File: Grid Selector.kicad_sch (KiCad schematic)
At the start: 122 parts, among them SW1 MX_SW_HS, SW10 MX_SW_HS, SW11 MX_SW_HS, SW12 MX_SW_HS, SW13 MX_SW_HS, SW14 MX_SW_HS, SW15 MX_SW_HS, SW16 MX_SW_HS, SW17 MX_SW_HS, SW18 MX_SW_HS, SW19 MX_SW_HS, SW2 MX_SW_HS, SW20 MX_SW_HS, SW21 MX_SW_HS, SW22 MX_SW_HS, SW23 MX_SW_HS, SW24 MX_SW_HS, SW25 MX_SW_HS, SW26 MX_SW_HS, SW27 MX_SW_HS, SW28 MX_SW_HS, SW29 MX_SW_HS, SW3 MX_SW_HS, SW30 MX_SW_HS, SW4 MX_SW_HS, SW5 MX_SW_HS, SW6 MX_SW_HS, SW7 MX_SW_HS, SW8 MX_SW_HS, SW9 MX_SW_HS, U1 Pico

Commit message: cleaned up pcb
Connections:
- net COL0: now also U1.12 (GPIO9); no longer U1.15 (GPIO11)
- net COL1: now also U1.11 (GPIO8); no longer U1.12 (GPIO9)
- net COL2: now also U1.10 (GPIO7); no longer U1.11 (GPIO8)
- net COL3: now also U1.9 (GPIO6); no longer U1.10 (GPIO7)
- net COL4: now also U1.7 (GPIO5); no longer U1.9 (GPIO6)
- net COL5: now also U1.6 (GPIO4); no longer U1.7 (GPIO5)
- net COL6: now also U1.5 (GPIO3); no longer U1.6 (GPIO4)
- net GND: now also U1.18 (GND); no longer U1.8 (GND)
- net ROW0: now also U1.15 (GPIO11); no longer U1.5 (GPIO3)
- net ROW1: now also U1.16 (GPIO12); no longer U1.14 (GPIO10)
- net ROW2: now also U1.17 (GPIO13); no longer U1.20 (GPIO15)
- net LED: now reaches LED1.3 (DIN)
- net LED: now also U1.14 (GPIO10)
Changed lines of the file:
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@@
     (stroke (width 0) (type default) (color 0 0 0 0))
   )
-  (wire (pts (xy 181.61 47.625) (xy 191.135 47.625))
+  (wire (pts (xy 181.61 73.025) (xy 191.135 73.025))
     (stroke (width 0) (type default) (color 0 0 0 0))
   )
@@
     (stroke (width 0) (type default) (color 0 0 0 0))
   )
-  (global_label "COL5" (shape input) (at 191.135 45.085 180) (fields_autoplaced)
-    (effects (font (size 1.27 1.27)) (justify right))
-    (property "Intersheet References" "${INTERSHEET_REFS}" (id 0) (at 183.8838 45.0056 0)
+  (global_label "COL5" (shape input) (at 191.135 42.545 180) (fields_autoplaced)
+    (effects (font (size 1.27 1.27)) (justify right))
+    (property "Intersheet References" "${INTERSHEET_REFS}" (id 0) (at 183.8838 42.4656 0)
       (effects (font (size 1.27 1.27)) (justify right) hide)
     )
@@
     )
   )
-  (global_label "COL1" (shape input) (at 191.135 57.785 180) (fields_autoplaced)
-    (effects (font (size 1.27 1.27)) (justify right))
-    (property "Intersheet References" "${INTERSHEET_REFS}" (id 0) (at 183.8838 57.7056 0)
+  (global_label "COL1" (shape input) (at 191.135 55.245 180) (fields_autoplaced)
+    (effects (font (size 1.27 1.27)) (justify right))
+    (property "Intersheet References" "${INTERSHEET_REFS}" (id 0) (at 183.8838 55.1656 0)
       (effects (font (size 1.27 1.27)) (justify right) hide)
     )
@@
     )
   )
-  (global_label "COL3" (shape input) (at 191.135 52.705 180) (fields_autoplaced)
-    (effects (font (size 1.27 1.27)) (justify right))
-    (property "Intersheet References" "${INTERSHEET_REFS}" (id 0) (at 183.8838 52.6256 0)
+  (global_label "COL3" (shape input) (at 191.135 50.165 180) (fields_autoplaced)
+    (effects (font (size 1.27 1.27)) (justify right))
+    (property "Intersheet References" "${INTERSHEET_REFS}" (id 0) (at 183.8838 50.0856 0)
+      (effects (font (size 1.27 1.27)) (justify right) hide)
+    )
+  )
+  (global_label "LED" (shape input) (at 19.685 102.87 180) (fields_autoplaced)
+    (effects (font (size 1.27 1.27)) (justify right))
+    (property "Intersheet References" "${INTERSHEET_REFS}" (id 0) (at 13.8248 102.7906 0)
       (effects (font (size 1.27 1.27)) (justify right) hide)
     )
@@
     )
   )
-  (global_label "COL2" (shape input) (at 191.135 55.245 180) (fields_autoplaced)
-    (effects (font (size 1.27 1.27)) (justify right))
-    (property "Intersheet References" "${INTERSHEET_REFS}" (id 0) (at 183.8838 55.1656 0)
+  (global_label "COL2" (shape input) (at 191.135 52.705 180) (fields_autoplaced)
+    (effects (font (size 1.27 1.27)) (justify right))
+    (property "Intersheet References" "${INTERSHEET_REFS}" (id 0) (at 183.8838 52.6256 0)
       (effects (font (size 1.27 1.27)) (justify right) hide)
     )
@@
     )
   )
-  (global_label "ROW2" (shape input) (at 191.135 78.105 180) (fields_autoplaced)
-    (effects (font (size 1.27 1.27)) (justify right))
-    (property "Intersheet References" "${INTERSHEET_REFS}" (id 0) (at 183.4605 78.0256 0)
+  (global_label "ROW2" (shape input) (at 191.135 70.485 180) (fields_autoplaced)
+    (effects (font (size 1.27 1.27)) (justify right))
+    (property "Intersheet References" "${INTERSHEET_REFS}" (id 0) (at 183.4605 70.4056 0)
       (effects (font (size 1.27 1.27)) (justify right) hide)
     )
@@
     )
   )
-  (global_label "COL4" (shape input) (at 191.135 50.165 180) (fields_autoplaced)
-    (effects (font (size 1.27 1.27)) (justify right))
-    (property "Intersheet References" "${INTERSHEET_REFS}" (id 0) (at 183.8838 50.0856 0)
-      (effects (font (size 1.27 1.27)) (justify right) hide)
-    )
-  )
-  (global_label "COL6" (shape input) (at 191.135 42.545 180) (fields_autoplaced)
-    (effects (font (size 1.27 1.27)) (justify right))
-    (property "Intersheet References" "${INTERSHEET_REFS}" (id 0) (at 183.8838 42.4656 0)
+  (global_label "LED" (shape input) (at 191.135 62.865 180) (fields_autoplaced)
+    (effects (font (size 1.27 1.27)) (justify right))
+    (property "Intersheet References" "${INTERSHEET_REFS}" (id 0) (at 185.2748 62.7856 0)
+      (effects (font (size 1.27 1.27)) (justify right) hide)
+    )
+  )
+  (global_label "COL4" (shape input) (at 191.135 45.085 180) (fields_autoplaced)
+    (effects (font (size 1.27 1.27)) (justify right))
+    (property "Intersheet References" "${INTERSHEET_REFS}" (id 0) (at 183.8838 45.0056 0)
+      (effects (font (size 1.27 1.27)) (justify right) hide)
+    )
+  )
+  (global_label "COL6" (shape input) (at 191.135 40.005 180) (fields_autoplaced)
+    (effects (font (size 1.27 1.27)) (justify right))
+    (property "Intersheet References" "${INTERSHEET_REFS}" (id 0) (at 183.8838 39.9256 0)
       (effects (font (size 1.27 1.27)) (justify right) hide)
     )
@@
     )
   )
-  (global_label "ROW0" (shape input) (at 191.135 40.005 180) (fields_autoplaced)
-    (effects (font (size 1.27 1.27)) (justify right))
-    (property "Intersheet References" "${INTERSHEET_REFS}" (id 0) (at 183.4605 39.9256 0)
-      (effects (font (size 1.27 1.27)) (justify right) hide)
-    )
-  )
-  (global_label "ROW1" (shape input) (at 191.135 62.865 180) (fields_autoplaced)
-    (effects (font (size 1.27 1.27)) (justify right))
-    (property "Intersheet References" "${INTERSHEET_REFS}" (id 0) (at 183.4605 62.7856 0)
+  (global_label "ROW0" (shape input) (at 191.135 65.405 180) (fields_autoplaced)
+    (effects (font (size 1.27 1.27)) (justify right))
+    (property "Intersheet References" "${INTERSHEET_REFS}" (id 0) (at 183.4605 65.3256 0)
+      (effects (font (size 1.27 1.27)) (justify right) hide)
+    )
+  )
+  (global_label "ROW1" (shape input) (at 191.135 67.945 180) (fields_autoplaced)
+    (effects (font (size 1.27 1.27)) (justify right))
+    (property "Intersheet References" "${INTERSHEET_REFS}" (id 0) (at 183.4605 67.8656 0)
       (effects (font (size 1.27 1.27)) (justify right) hide)
     )
@@
     )
   )
-  (global_label "COL0" (shape input) (at 191.135 65.405 180) (fields_autoplaced)
-    (effects (font (size 1.27 1.27)) (justify right))
-    (property "Intersheet References" "${INTERSHEET_REFS}" (id 0) (at 183.8838 65.3256 0)
+  (global_label "COL0" (shape input) (at 191.135 57.785 180) (fields_autoplaced)
+    (effects (font (size 1.27 1.27)) (justify right))
+    (property "Intersheet References" "${INTERSHEET_REFS}" (id 0) (at 183.8838 57.7056 0)
       (effects (font (size 1.27 1.27)) (justify right) hide)
     )
@@
     (pin "2")
   )
-  (symbol (lib_id "power:GND") (at 181.61 47.625 0) (unit 1)
-    (in_bom yes) (on_board yes) (fields_autoplaced)
-    (property "Reference" "#PWR0101" (id 0) (at 181.61 53.975 0)
-      (effects (font (size 1.27 1.27)) hide)
-    )
-    (property "Value" "GND" (id 1) (at 181.61 52.07 0))
-    (property "Footprint" "" (id 2) (at 181.61 47.625 0)
-      (effects (font (size 1.27 1.27)) hide)
-    )
-    (property "Datasheet" "" (id 3) (at 181.61 47.625 0)
-      (effects (font (size 1.27 1.27)) hide)
-    )
+  (symbol (lib_id "power:GND") (at 181.61 73.025 0) (unit 1)
+    (in_bom yes) (on_board yes) (fields_autoplaced)
+    (property "Reference" "#PWR0101" (id 0) (at 181.61 79.375 0)
+      (effects (font (size 1.27 1.27)) hide)
+    )
+    (property "Value" "GND" (id 1) (at 181.61 77.47 0))
+    (property "Footprint" "" (id 2) (at 181.61 73.025 0)
+      (effects (font (size 1.27 1.27)) hide)
+    )
+    (property "Datasheet" "" (id 3) (at 181.61 73.025 0)
+      (effects (font (size 1.27 1.27)) hide)
+    )

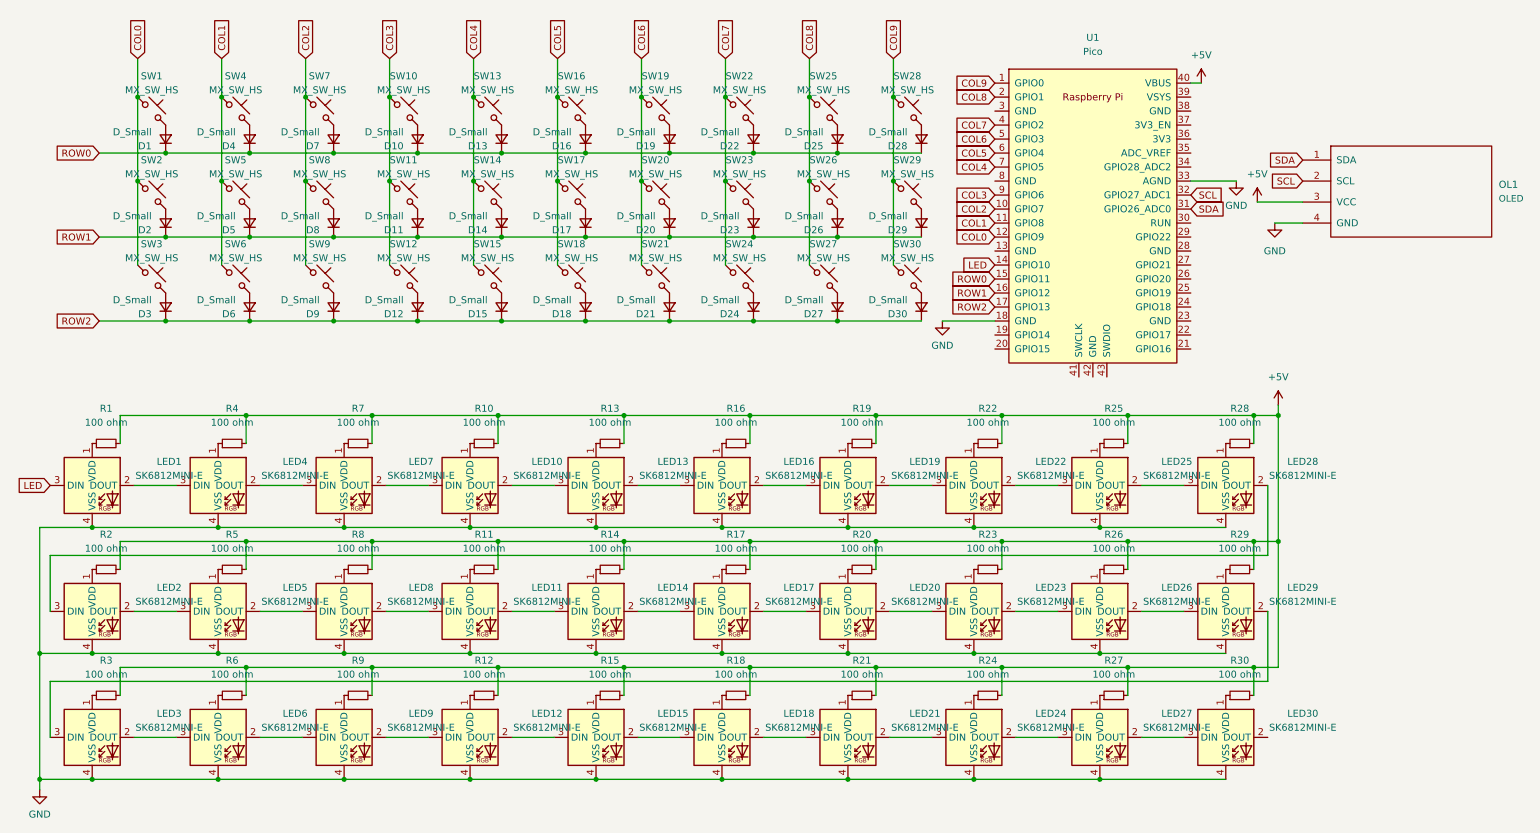
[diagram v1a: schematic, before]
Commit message: reduced the size to 15 keys
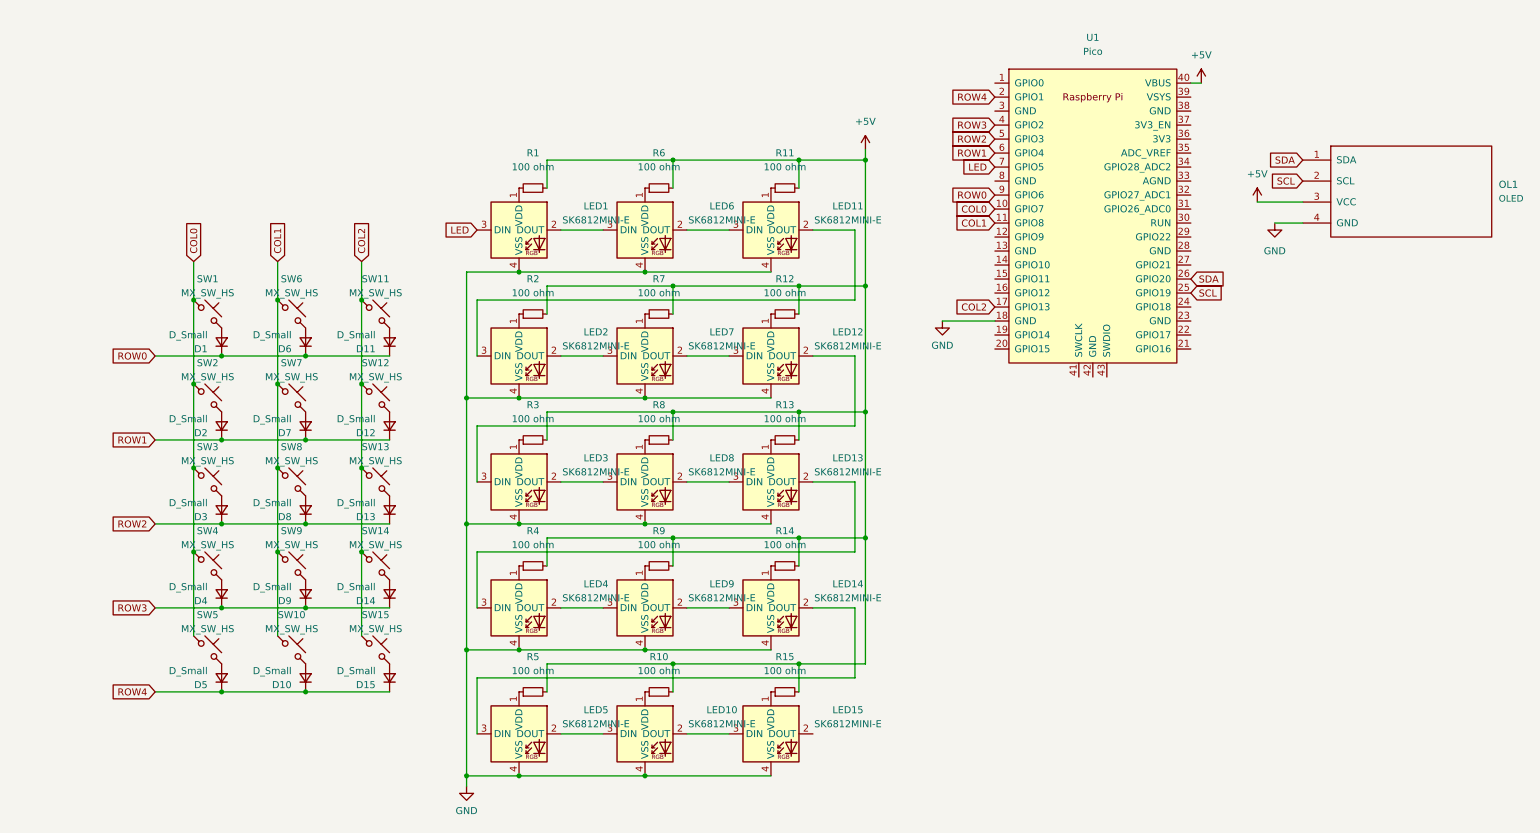
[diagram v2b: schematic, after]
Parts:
- removed D16, D17, D18, D19, D20, D21, D22, D23, D24, D25, D26, D27, D28, D29, D30: D_Small, Diode_SMD:D_SOD-123, symbol Device:D_Small
- removed LED16, LED17, LED18, LED19, LED20, LED21, LED22, LED23, LED24, LED25, LED26, LED27, LED28, LED29, LED30: SK6812MINI-E, marbastlib-various:LED_6028R, symbol marbastlib-various:SK6812MINI-E
- removed R16, R17, R18, R19, R20, R21, R22, R23, R24, R25, R26, R27, R28, R29, R30: 100 ohm, Resistor_SMD:R_0805_2012Metric, symbol Device:R_Small
- removed SW16, SW17, SW18, SW19, SW20, SW21, SW22, SW23, SW24, SW25, SW26, SW27, SW28, SW29, SW30: MX_SW_HS, marbastlib-mx:SW_MX_HS_1u, symbol marbastlib-mx:MX_SW_HS
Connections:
- net COL5 is gone; now on net ROW1: U1.6 (GPIO4)
- net COL6 is gone; now on net ROW2: U1.5 (GPIO3)
- net COL0: now also SW4.1, SW5.1, U1.10 (GPIO7); no longer U1.12 (GPIO9)
- net COL1: now also SW10.1, SW7.1, SW8.1, SW9.1; no longer SW4.1, SW5.1
- net COL2: now also SW11.1, SW12.1, SW13.1, SW14.1, SW15.1, U1.17 (GPIO13); no longer SW7.1, SW8.1, SW9.1, U1.10 (GPIO7)
- net GND: no longer U1.33 (AGND)
- net LED: now also U1.7 (GPIO5); no longer U1.14 (GPIO10)
- net ROW0: now also D11.1 (K), D6.1 (K), U1.9 (GPIO6); no longer D10.1 (K), D13.1 (K), D4.1 (K), D7.1 (K), U1.15 (GPIO11)
- net ROW1: now also D12.1 (K), D7.1 (K); no longer D11.1 (K), D14.1 (K), D5.1 (K), D8.1 (K), U1.16 (GPIO12)
- net ROW2: now also D13.1 (K), D8.1 (K); no longer D12.1 (K), D15.1 (K), D6.1 (K), D9.1 (K), U1.17 (GPIO13)
- net SCL: now also U1.25 (GPIO19); no longer U1.32 (GPIO27_ADC1)
- net SDA: now also U1.26 (GPIO20); no longer U1.31 (GPIO26_ADC0)
- net at LED9.2 (DOUT): now also LED14.3 (DIN); no longer LED12.3 (DIN)
- net at LED9.3 (DIN): now also LED4.2 (DOUT); no longer LED6.2 (DOUT)
- net at LED7.2 (DOUT): now also LED12.3 (DIN); no longer LED10.3 (DIN)
- net at LED7.3 (DIN): now also LED2.2 (DOUT); no longer LED4.2 (DOUT)
- net at LED12.2 (DOUT): now also LED3.3 (DIN); no longer LED15.3 (DIN)
- net at LED8.2 (DOUT): now also LED13.3 (DIN); no longer LED11.3 (DIN)
- net at LED8.3 (DIN): now also LED3.2 (DOUT); no longer LED5.2 (DOUT)
- net at LED14.2 (DOUT): now also LED5.3 (DIN)
- net at LED10.2 (DOUT): now also LED15.3 (DIN); no longer LED13.3 (DIN)
- net at LED13.2 (DOUT): now also LED4.3 (DIN)
- net at LED1.2 (DOUT): now also LED6.3 (DIN); no longer LED4.3 (DIN)
- net at LED11.2 (DOUT): now also LED2.3 (DIN); no longer LED14.3 (DIN)
- removed net COL3: SW10.1, SW11.1, SW12.1, U1.9 (GPIO6)
- removed net COL4: SW13.1, SW14.1, SW15.1, U1.7 (GPIO5)
- net COL7 renamed ROW3
- net ROW3: now also D14.1 (K), D4.1 (K), D9.1 (K)
- net COL8 renamed ROW4
- net ROW4: now also D10.1 (K), D15.1 (K), D5.1 (K)
- net COL9: no longer names the net of U1.1 (GPIO0)
- new net: LED10.3 (DIN), LED5.2 (DOUT)
- new net: LED11.3 (DIN), LED6.2 (DOUT)
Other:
- moved on the sheet: D1, D10, D11, D12, D13, D14, D15, D2, D3, D4, D5, D6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
